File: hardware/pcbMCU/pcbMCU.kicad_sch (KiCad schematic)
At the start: 31 parts, among them J1 Conn_01x02, J2 Conn_01x04, J3 Conn_01x03, SW1 SW_SPDT, U1 AMS1117-3.3, U2 STM32F103C8Tx, U3 Ai-Thinker-Ra-02, Y1 8MHz

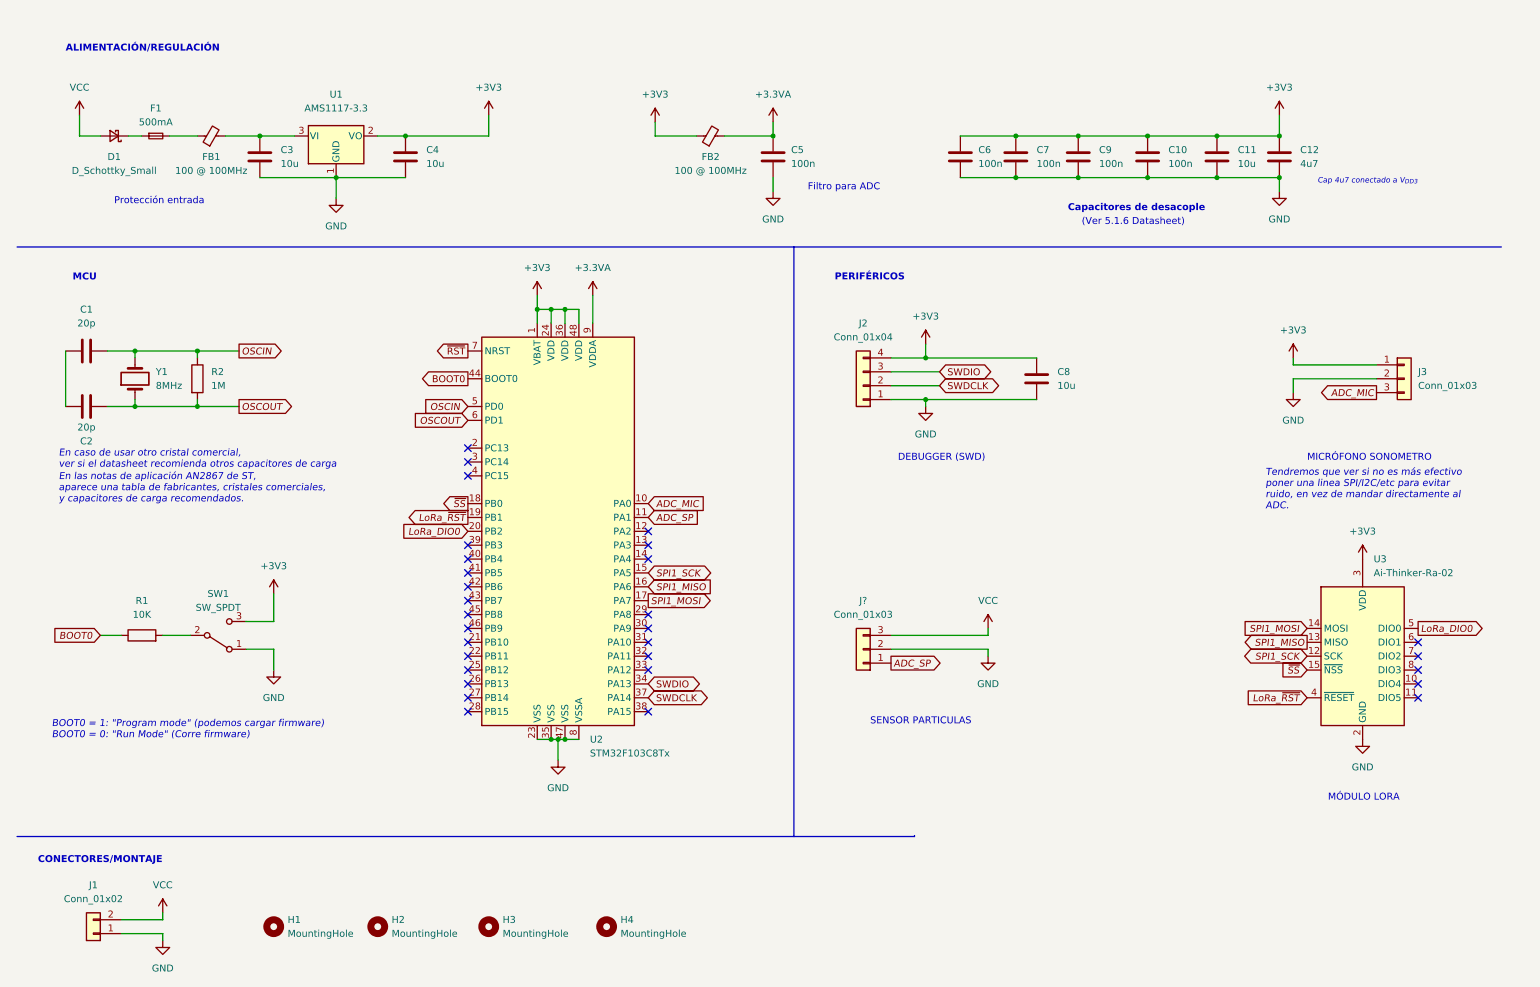
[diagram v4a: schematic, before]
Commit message: Cambio de MCU a STM32L4 + Firmware Inicial
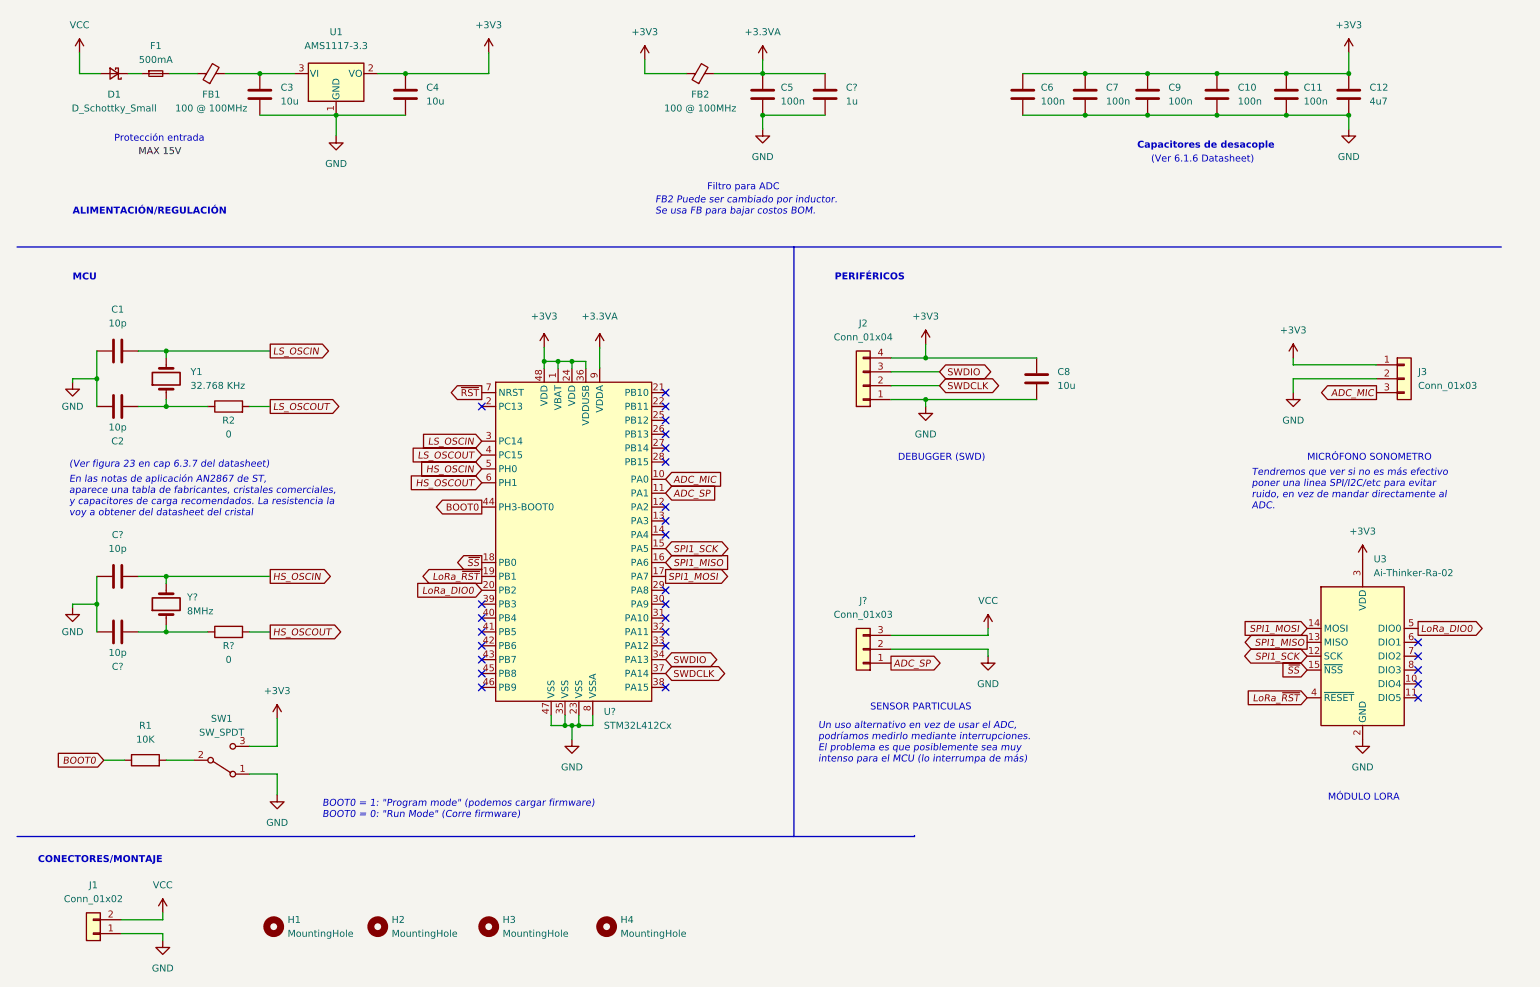
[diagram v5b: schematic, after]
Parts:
- removed U2: STM32F103C8Tx, Package_QFP:LQFP-48_7x7mm_P0.5mm, symbol MCU_ST_STM32F1:STM32F103C8Tx
- added C? (x2): 10p, symbol Device:C
- added C?: 1u, symbol Device:C
- added R?: 0, symbol Device:R
- added U?: STM32L412Cx, symbol MCU_ST_STM32L4:STM32L412Cx
- added Y?: 8MHz, symbol Device:Crystal
- C1, C2: value 20p -> 10p
- C11: value 10u -> 100n
- R2: value 1M -> 0
- Y1: value 8MHz -> 32.768 KHz
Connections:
- net +3.3VA: now also C?.1, U?.9 (VDDA)
- net +3V3: now also U?.1 (VBAT), U?.24 (VDD), U?.36 (VDDUSB), U?.48 (VDD)
- net ADC_MIC: now also U?.10 (PA0)
- net ADC_SP: now also U?.11 (PA1)
- net BOOT0: now also U?.44 (PH3-BOOT0)
- net GND: now also C1.1, C2.1, C?.1, C?.1, C?.2, U?.23 (VSS), U?.35 (VSS), U?.47 (VSS), U?.8 (VSSA)
- net LoRa_DIO0: now also U?.20 (PB2)
- net LoRa_~{RST}: now also U?.19 (PB1)
- net SPI1_MISO: now also U?.16 (PA6)
- net SPI1_MOSI: now also U?.17 (PA7)
- net SPI1_SCK: now also U?.15 (PA5)
- net SWDCLK: now also U?.37 (PA14)
- net SWDIO: now also U?.34 (PA13)
- net ~{RST}: now also U?.7 (NRST)
- net ~{SS}: now also U?.18 (PB0)
- net OSCIN renamed LS_OSCIN
- net LS_OSCIN: now also U?.3 (PC14); no longer R2.1
- net OSCOUT: no longer names the net of C2.2, Y1.1
- net OSCOUT: now also R2.1; no longer R2.2
- new net: C?.2, R?.1, Y?.1
- new net HS_OSCIN: C?.2, U?.5 (PH0), Y?.2
- new net HS_OSCOUT: R?.2, U?.6 (PH1)
- new net LS_OSCOUT: R2.2, U?.4 (PC15)
- no-connect marks 30 -> 28
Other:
- note added: "(Ver 6.1.6 Datasheet)"
- note added: "(Ver figura 23 en cap 6.3.7 del datasheet)"
- note added: "En las notas de aplicación AN2867 de ST, aparece una tabla de fabricantes, cristales comerciales, y capacitores de carga recomendados. La resistencia la voy a obtener del datasheet del cristal"
- note added: "FB2 Puede ser cambiado por inductor. Se usa FB para bajar costos BOM."
- note added: "Un uso alternativo en vez de usar el ADC, podríamos medirlo mediante interrupciones. El problema es que posiblemente sea muy intenso para el MCU (lo interrumpa de más)"
- note removed: "(Ver 5.1.6 Datasheet)"
- note removed: "Cap 4u7 conectado a V_{DD3}"
- note removed: "En caso de usar otro cristal comercial, ver si el datasheet recomienda otros capacitores de carga"
- note removed: "En las notas de aplicación AN2867 de ST, aparece una tabla de fabricantes, cristales comerciales, y capacitores de carga recomendados."
- moved on the sheet: C1, C10, C11, C12, C2, C3, C4, C5, C6, C7, C9, D1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

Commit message: Añadido convertidor buck para batería
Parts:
- removed D1: D_Schottky_Small, symbol Device:D_Schottky_Small
- removed F1: 500mA, symbol Device:Fuse_Small
- removed FB1: 100 @ 100MHz, symbol Device:FerriteBead_Small
- added C? (x2): 22u, symbol Device:C_Small
- added C?: 100n, symbol Device:C_Small
- added C?: 10u, symbol Device:C_Small
- added D?: D_Schottky_Small, symbol Device:D_Schottky_Small
- added F?: 500mA, symbol Device:Fuse_Small
- added FB?: 100 @ 100MHz, symbol Device:FerriteBead_Small
- added L?: 3u3, symbol Device:L_Small
- added R?: 52K3, symbol Device:R
- added R?: 10K, symbol Device:R
- added U?: AP62300, Package_TO_SOT_SMD:SOT-563, symbol Regulator_Switching:AP62300Z6
- C1, C10, C11, C12, C2, C3, C4, C5, C6, C7, C8, C9, C? (x3): symbol Device:C -> Device:C_Small
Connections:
- net +3V3: no longer J3.1 (Pin_1)
- net GND: now also C?.2, C?.2, C?.2, R?.1, U?.3 (GND)
- net VCC: now also J3.1 (Pin_1), D?.2 (A)
- net +5V: now reaches C3.1, U1.3 (VI)
- net +5V: now also C?.1, C?.1, L?.2, R?.2
- new net: D?.1 (K), F?.1
- new net: F?.2, FB?.1
- new net: C?.1, L?.1, U?.2 (SW)
- new net: C?.1, FB?.2, U?.1 (VIN)
- new net: C?.2, U?.4 (BST)
- new net: R?.1, R?.2, U?.6 (FB)
- no-connect marks 28 -> 29
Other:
- note added: "(Se puede programar EN para protección a baja tensión)"
- note added: "R1 = R2*(V_{OUT}/V_{FB}-1)"
- moved on the sheet: C10, C11, C12, C3, C4, C5, C6, C7, C9, C?, FB2, U1

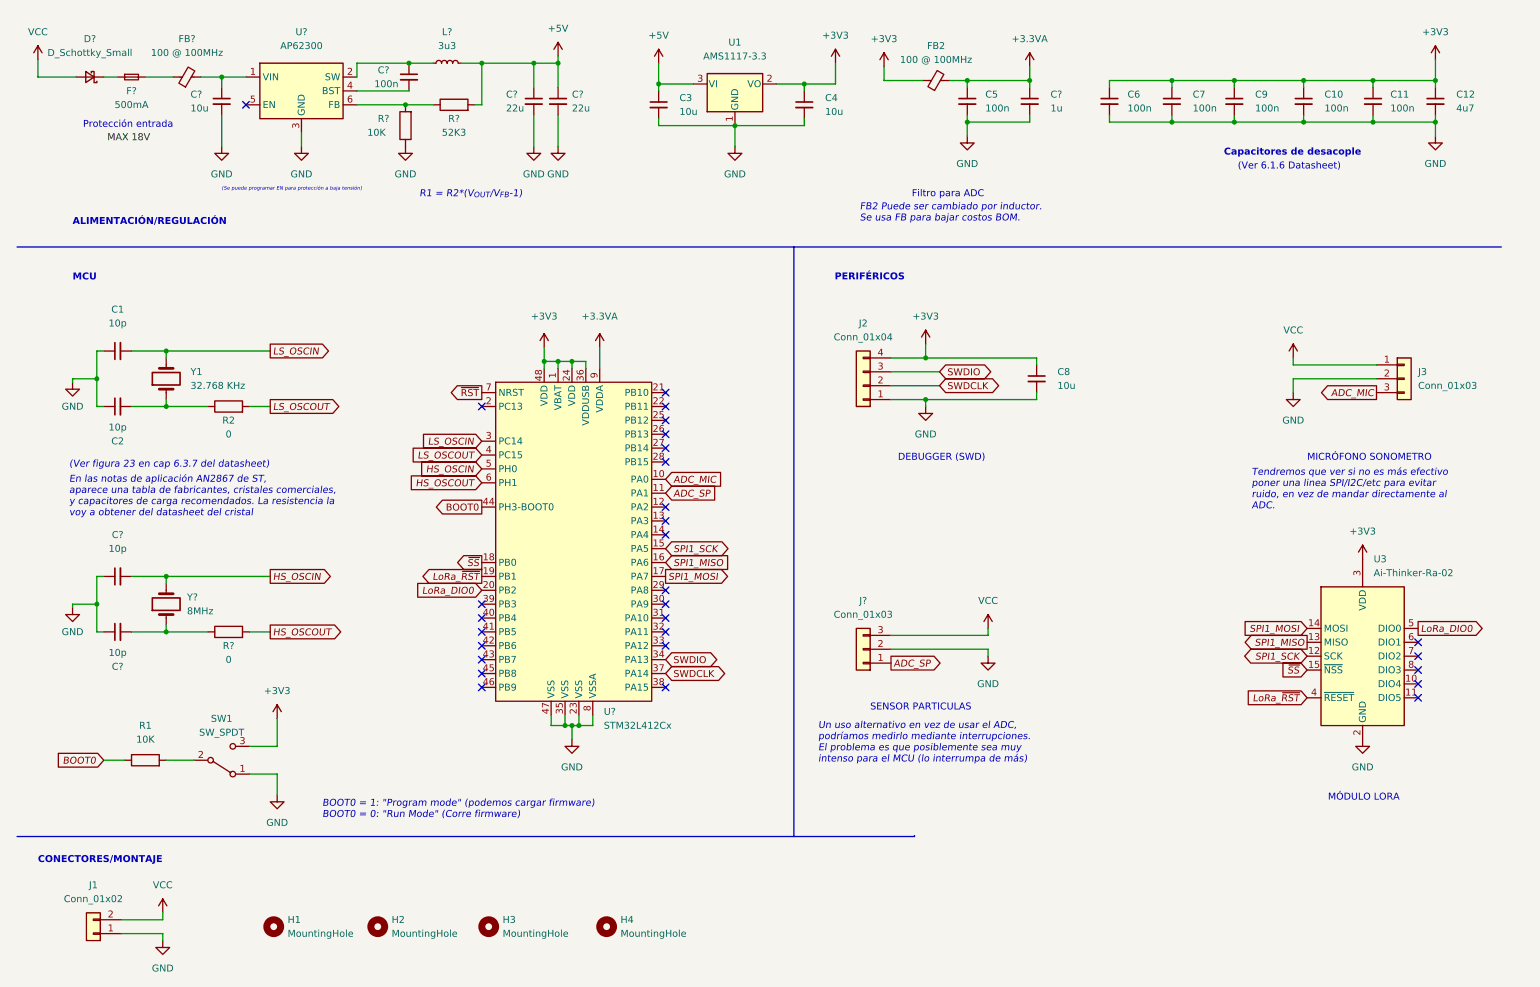
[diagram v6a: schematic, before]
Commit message: Cambio conector SP. Añadido módulo LoRa 915Mhz
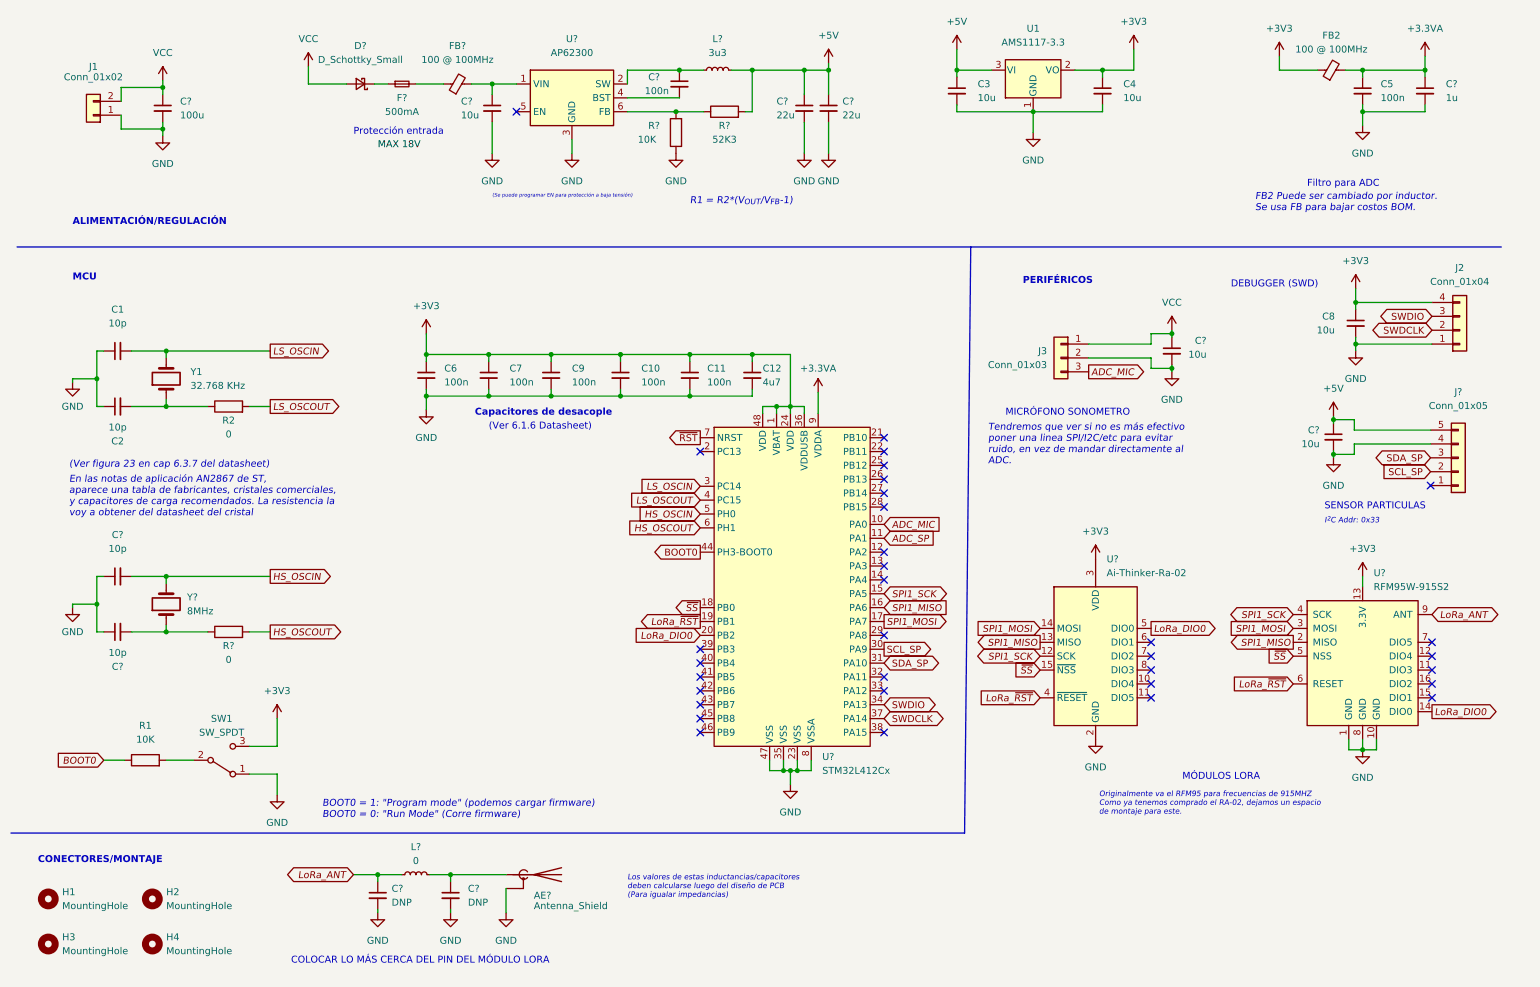
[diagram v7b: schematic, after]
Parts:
- removed J?: Conn_01x03, symbol Connector_Generic:Conn_01x03
- removed U3: Ai-Thinker-Ra-02, RF_Module:Ai-Thinker-Ra-01-LoRa, symbol RF_Module:Ai-Thinker-Ra-02
- added AE?: Antenna_Shield, symbol Device:Antenna_Shield
- added C?: 100u, symbol Device:C_Small
- added C? (x2): 10u, symbol Device:C_Small
- added C? (x2): DNP, symbol Device:C_Small
- added J?: Conn_01x05, Connector_JST:JST_GH_SM05B-GHS-TB_1x05-1MP_P1.25mm_Horizontal, symbol Connector_Generic:Conn_01x05
- added L?: 0, symbol Device:L_Small
- added U?: RFM95W-915S2, symbol RF_Module:RFM95W-915S2
- added U?: Ai-Thinker-Ra-02, RF_Module:Ai-Thinker-Ra-01-LoRa, symbol RF_Module:Ai-Thinker-Ra-02
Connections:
- net +3V3: now also U?.13 (3.3V), U?.3 (VDD)
- net +5V: now also C?.1, J?.5 (Pin_5)
- net GND: now also AE?.2 (Shield), C?.2, C?.2, C?.2, C?.2, C?.2, J?.4 (Pin_4), U?.1 (GND), U?.1 (GND), U?.10 (GND), U?.16 (GND), U?.2 (GND), U?.8 (GND), U?.9 (GND)
- net LoRa_DIO0: now also U?.14 (DIO0), U?.5 (DIO0)
- net LoRa_~{RST}: now also U?.4 (~{RESET}), U?.6 (RESET)
- net SPI1_MISO: now also U?.13 (MISO), U?.2 (MISO)
- net SPI1_MOSI: now also U?.14 (MOSI), U?.3 (MOSI)
- net SPI1_SCK: now also U?.12 (SCK), U?.4 (SCK)
- net VCC: now also C?.1, C?.1
- net ~{SS}: now also U?.15 (~{NSS}), U?.5 (NSS)
- net SCL_SP: now reaches U?.30 (PA9)
- net SCL_SP: now also J?.2 (Pin_2)
- net SDA_SP: now reaches U?.31 (PA10)
- net SDA_SP: now also J?.3 (Pin_3)
- new net: AE?.1 (A), C?.1, L?.2
- new net LoRa_ANT: C?.1, L?.1, U?.9 (ANT)
- no-connect marks 29 -> 33
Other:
- note added: "COLOCAR LO MÁS CERCA DEL PIN DEL MÓDULO LORA"
- note added: "I^{2}C Addr: 0x33"
- note added: "Los valores de estas inductancias/capacitores deben calcularse luego del diseño de PCB (Para igualar impedancias)"
- note added: "MÓDULOS LORA"
- note added: "Originalmente va el RFM95 para frecuencias de 915MHZ Como ya tenemos comprado el RA-02, dejamos un espacio de montaje para este."
- note removed: "MÓDULO LORA"
- note removed: "Un uso alternativo en vez de usar el ADC, podríamos medirlo mediante interrupciones. El problema es que posiblemente sea muy intenso para el MCU (lo interrumpa de más)"
- moved on the sheet: C10, C11, C12, C3, C4, C5, C6, C7, C8, C9, C?, D?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
